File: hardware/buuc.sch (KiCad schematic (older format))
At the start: 18 parts, among them P1 USB_OTG, P2 CONN_01X02, Q1 NDS8434, U1 BOOST_REGULATOR, U2 MCP73842-840I/UN

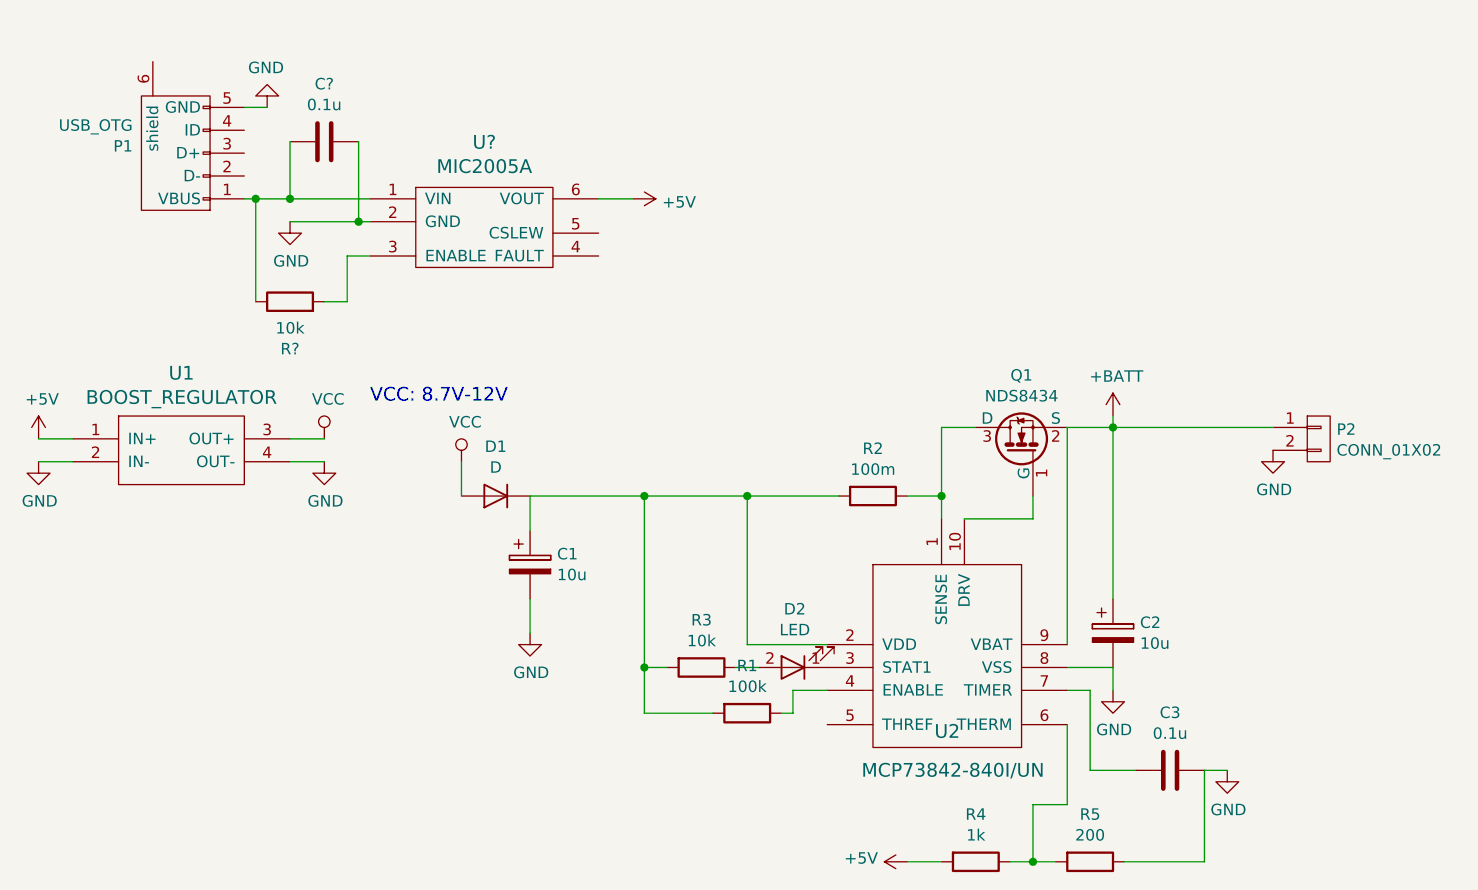
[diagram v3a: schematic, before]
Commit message: Swapping resistor footprint for one that's a bit easier to solder onto a milled board; minor move of the USB connector.
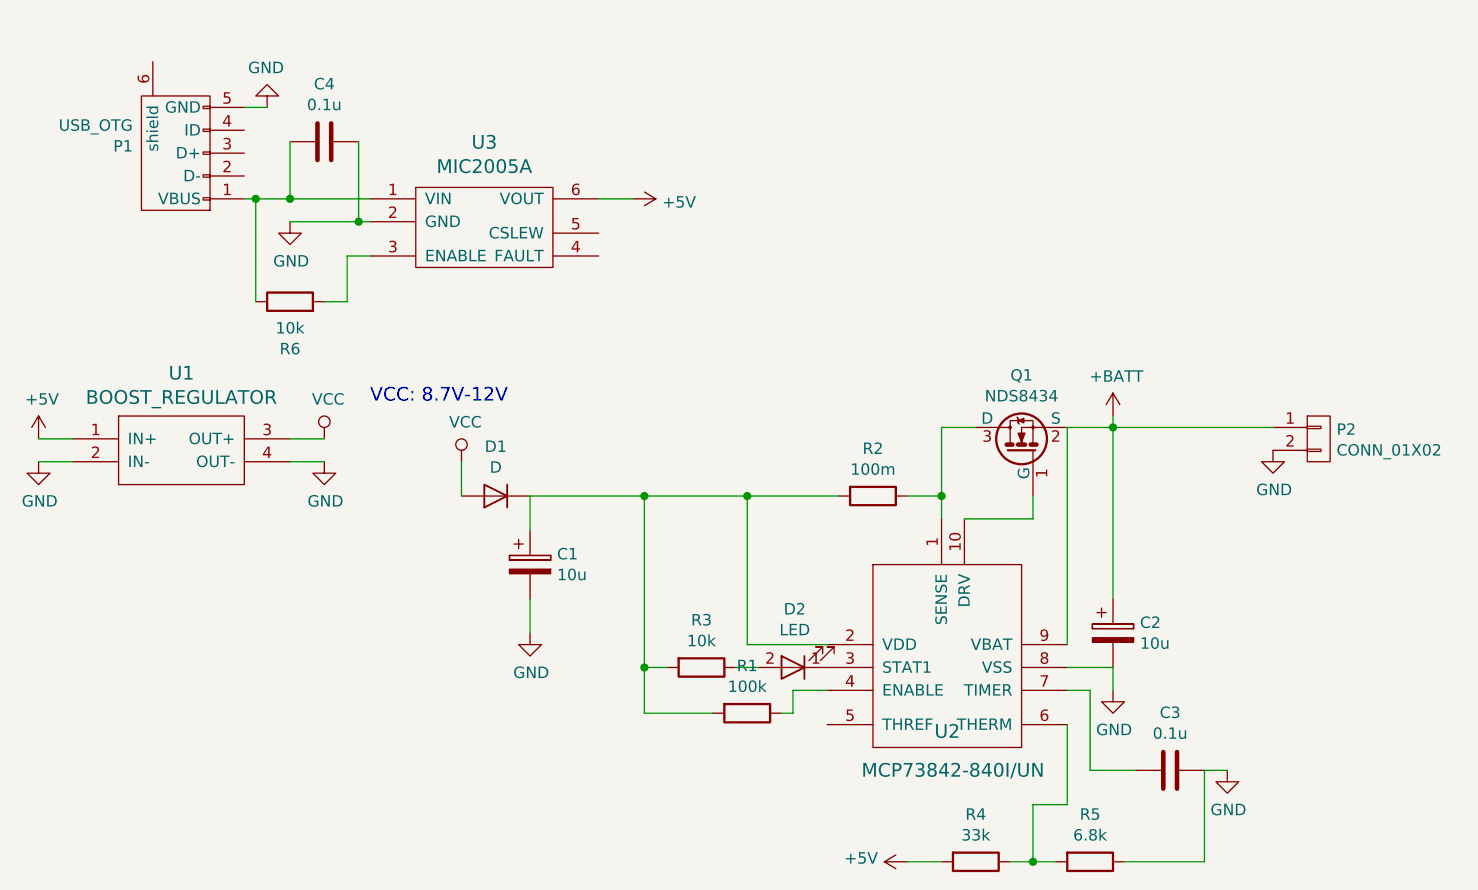
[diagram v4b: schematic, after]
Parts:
- C3: footprint KiCad/Capacitors_SMD.pretty:C_0805_HandSoldering -> coddingtonbear/coddingtonbear.pretty:0805_Milling
- C4: renamed from C?; footprint KiCad/Capacitors_SMD.pretty:C_0805_HandSoldering -> coddingtonbear/coddingtonbear.pretty:0805_Milling
- D2: footprint adamgreig/agg-kicad/agg.pretty:0805-LED -> coddingtonbear/coddingtonbear.pretty:0805_Milling
- R1, R2, R3: footprint apexelectrix/apex-smd-resistors.pretty:R_0805_HandSoldering -> coddingtonbear/coddingtonbear.pretty:0805_Milling
- R4: value 1k -> 33k; footprint apexelectrix/apex-smd-resistors.pretty:R_0805_HandSoldering -> coddingtonbear/coddingtonbear.pretty:0805_Milling
- R5: value 200 -> 6.8k; footprint apexelectrix/apex-smd-resistors.pretty:R_0805_HandSoldering -> coddingtonbear/coddingtonbear.pretty:0805_Milling
- R6: renamed from R?; footprint apexelectrix/apex-smd-resistors.pretty:R_0805_HandSoldering -> coddingtonbear/coddingtonbear.pretty:0805_Milling
- U3: renamed from U?; footprint (none) -> adamgreig/agg-kicad/agg.pretty:SOT-23-6
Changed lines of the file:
@@
 F 0 "R2" V 4393 2950 50  0000 C CNN
 F 1 "100m" V 4484 2950 50  0000 C CNN
-F 2 "apexelectrix/apex-smd-resistors.pretty:R_0805_HandSoldering" V 4530 2950 50  0001 C CNN
+F 2 "coddingtonbear/coddingtonbear.pretty:0805_Milling" V 4530 2950 50  0001 C CNN
 F 3 "" H 4600 2950 50  0000 C CNN
 	1    4600 2950
@@
 F 0 "D2" H 4242 3445 50  0000 C CNN
 F 1 "LED" H 4242 3536 50  0000 C CNN
-F 2 "adamgreig/agg-kicad/agg.pretty:0805-LED" H 4250 3700 50  0001 C CNN
+F 2 "coddingtonbear/coddingtonbear.pretty:0805_Milling" H 4250 3700 50  0001 C CNN
 F 3 "" H 4250 3700 50  0000 C CNN
 	1    4250 3700
@@
 F 0 "R1" V 3843 3900 50  0000 C CNN
 F 1 "100k" V 3934 3900 50  0000 C CNN
-F 2 "apexelectrix/apex-smd-resistors.pretty:R_0805_HandSoldering" V 3980 3900 50  0001 C CNN
+F 2 "coddingtonbear/coddingtonbear.pretty:0805_Milling" V 3980 3900 50  0001 C CNN
 F 3 "" H 4050 3900 50  0000 C CNN
 	1    4050 3900
@@
 F 0 "R3" V 3643 3700 50  0000 C CNN
 F 1 "10k" V 3734 3700 50  0000 C CNN
-F 2 "apexelectrix/apex-smd-resistors.pretty:R_0805_HandSoldering" V 3780 3700 50  0001 C CNN
+F 2 "coddingtonbear/coddingtonbear.pretty:0805_Milling" V 3780 3700 50  0001 C CNN
 F 3 "" H 3850 3700 50  0000 C CNN
 	1    3850 3700
@@
 F 0 "C3" V 5648 4150 50  0000 C CNN
 F 1 "0.1u" V 5739 4150 50  0000 C CNN
-F 2 "KiCad/Capacitors_SMD.pretty:C_0805_HandSoldering" H 5938 4000 50  0001 C CNN
+F 2 "coddingtonbear/coddingtonbear.pretty:0805_Milling" H 5938 4000 50  0001 C CNN
 F 3 "" H 5900 4150 50  0000 C CNN
 	1    5900 4150
@@
 P 5050 4550
 F 0 "R4" V 4843 4550 50  0000 C CNN
-F 1 "1k" V 4934 4550 50  0000 C CNN
-F 2 "apexelectrix/apex-smd-resistors.pretty:R_0805_HandSoldering" V 4980 4550 50  0001 C CNN
+F 1 "33k" V 4934 4550 50  0000 C CNN
+F 2 "coddingtonbear/coddingtonbear.pretty:0805_Milling" V 4980 4550 50  0001 C CNN
 F 3 "" H 5050 4550 50  0000 C CNN
 	1    5050 4550
@@
 P 5550 4550
 F 0 "R5" V 5343 4550 50  0000 C CNN
-F 1 "200" V 5434 4550 50  0000 C CNN
-F 2 "apexelectrix/apex-smd-resistors.pretty:R_0805_HandSoldering" V 5480 4550 50  0001 C CNN
+F 1 "6.8k" V 5434 4550 50  0000 C CNN
+F 2 "coddingtonbear/coddingtonbear.pretty:0805_Milling" V 5480 4550 50  0001 C CNN
 F 3 "" H 5550 4550 50  0000 C CNN
 	1    5550 4550
@@
 	4750 4550 4900 4550
 $Comp
-L MIC2005A U?
+L MIC2005A U3
 U 1 1 59BADA49
 P 2900 1750
-F 0 "U?" H 2900 2097 60  0000 C CNN
+F 0 "U3" H 2900 2097 60  0000 C CNN
 F 1 "MIC2005A" H 2900 1991 60  0000 C CNN
-F 2 "" H 2900 1750 60  0001 C CNN
+F 2 "adamgreig/agg-kicad/agg.pretty:SOT-23-6" H 2900 1750 60  0001 C CNN
 F 3 "" H 2900 1750 60  0001 C CNN
 	1    2900 1750
@@
 	3550 1650 3400 1650
 $Comp
-L GND #PWR?
+L GND #PWR014
 U 1 1 59BADB64
 P 2050 1750
-F 0 "#PWR?" H 2050 1500 50  0001 C CNN
+F 0 "#PWR014" H 2050 1500 50  0001 C CNN
 F 1 "GND" H 2055 1577 50  0000 C CNN
 F 2 "" H 2050 1750 50  0000 C CNN
@@
 	2400 1750 2050 1750
 $Comp
-L R R?
+L R R6
 U 1 1 59BADC60
 P 2050 2100
-F 0 "R?" V 1843 2100 50  0000 C CNN
+F 0 "R6" V 1843 2100 50  0000 C CNN
 F 1 "10k" V 1934 2100 50  0000 C CNN
-F 2 "apexelectrix/apex-smd-resistors.pretty:R_0805_HandSoldering" V 1980 2100 50  0001 C CNN
+F 2 "coddingtonbear/coddingtonbear.pretty:0805_Milling" V 1980 2100 50  0001 C CNN
 F 3 "" H 2050 2100 50  0000 C CNN
 	1    2050 2100
@@
 Connection ~ 1900 1650
 $Comp
-L C C?
+L C C4
 U 1 1 59BAE16D
 P 2200 1400
-F 0 "C?" V 1948 1400 50  0000 C CNN
+F 0 "C4" V 1948 1400 50  0000 C CNN
 F 1 "0.1u" V 2039 1400 50  0000 C CNN
-F 2 "KiCad/Capacitors_SMD.pretty:C_0805_HandSoldering" H 2238 1250 50  0001 C CNN
+F 2 "coddingtonbear/coddingtonbear.pretty:0805_Milling" H 2238 1250 50  0001 C CNN
 F 3 "" H 2200 1400 50  0000 C CNN
 	1    2200 1400

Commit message: Apparently: active low.  FFS.
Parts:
- U3: symbol MIC2005A -> MIC2005A-RESCUE-buuc
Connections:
- net GND: now also R6.1
- net at C4.2, P1.1 (VBUS), U3.1 (VIN): no longer R6.1
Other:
- moved on the sheet: R6
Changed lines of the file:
@@
 EESchema Schematic File Version 2
+LIBS:buuc-rescue
 LIBS:power
 LIBS:device
@@
 	4750 4550 4900 4550
 $Comp
-L MIC2005A U3
+L MIC2005A-RESCUE-buuc U3
 U 1 1 59BADA49
 P 2900 1750
@@
 L GND #PWR014
 U 1 1 59BADB64
-P 2050 1750
-F 0 "#PWR014" H 2050 1500 50  0001 C CNN
-F 1 "GND" H 2055 1577 50  0000 C CNN
-F 2 "" H 2050 1750 50  0000 C CNN
-F 3 "" H 2050 1750 50  0000 C CNN
-	1    2050 1750
-	1    0    0    -1
-$EndComp
-Wire Wire Line
-	2400 1750 2050 1750
+P 1800 2100
+F 0 "#PWR014" H 1800 1850 50  0001 C CNN
+F 1 "GND" H 1805 1927 50  0000 C CNN
+F 2 "" H 1800 2100 50  0000 C CNN
+F 3 "" H 1800 2100 50  0000 C CNN
+	1    1800 2100
+	1    0    0    -1
+$EndComp
+Wire Wire Line
+	1800 1750 2400 1750
 $Comp
 L R R6
 U 1 1 59BADC60
-P 2050 2100
-F 0 "R6" V 1843 2100 50  0000 C CNN
-F 1 "10k" V 1934 2100 50  0000 C CNN
-F 2 "coddingtonbear/coddingtonbear.pretty:0805_Milling" V 1980 2100 50  0001 C CNN
-F 3 "" H 2050 2100 50  0000 C CNN
-	1    2050 2100
-	0    -1   -1   0
-$EndComp
-Wire Wire Line
-	2200 2100 2300 2100
-Wire Wire Line
-	2300 2100 2300 1900
-Wire Wire Line
-	2300 1900 2400 1900
-Wire Wire Line
-	1900 2100 1900 1650
-Connection ~ 1900 1650
+P 2150 1950
+F 0 "R6" V 1943 1950 50  0000 C CNN
+F 1 "10k" V 2034 1950 50  0000 C CNN
+F 2 "coddingtonbear/coddingtonbear.pretty:0805_Milling" V 2080 1950 50  0001 C CNN
+F 3 "" H 2150 1950 50  0000 C CNN
+	1    2150 1950
+	1    0    0    -1
+$EndComp
 $Comp
 L C C4
@@
 	2050 1400 2050 1650
 Connection ~ 2050 1650
+Wire Wire Line
+	2150 1800 2150 1750
+Connection ~ 2150 1750
+Wire Wire Line
+	2150 2100 2400 2100
+Wire Wire Line
+	2400 2100 2400 1900
+Wire Wire Line
+	1800 1750 1800 2100
 $EndSCHEMATC

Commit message: Adding extra pads allowing me to fine-tune the consumed current; adding unpopulated bypass resistor around the MIC2005.
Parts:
- P1: symbol USB_OTG -> USB_OTG-RESCUE-buuc
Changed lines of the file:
@@
 LIBS:contrib
 LIBS:valves
-LIBS:coddingtonbear
 LIBS:buuc-cache
 EELAYER 26 0
@@
 $EndDescr
 $Comp
-L USB_OTG P1
+L USB_OTG-RESCUE-buuc P1
 U 1 1 59AF531F
 P 1550 1450

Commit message: fixup! Adding extra pads allowing me to fine-tune the consumed current; adding unpopulated bypass resistor around the MIC2005.
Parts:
- added R?: 100m, coddingtonbear/coddingtonbear.pretty:0805_Milling, symbol R
- added R? (x7): 0, coddingtonbear/coddingtonbear.pretty:0805_Milling, symbol R
- added R?: EMPTY, coddingtonbear/coddingtonbear.pretty:0805_Milling, symbol R
- R2: value 100m -> 0
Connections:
- net +5V: now also R?.2
- net at C4.2, P1.1 (VBUS), U3.1 (VIN): now also R?.1
- net at Q1.3 (D), U2.1 (SENSE): now also R?.2; no longer R2.1
- net at C1.1, D1.1 (K), R1.2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: now also R?.1; no longer R2.2
- new net: R2.1, R?.2
- new net: R2.2, R?.2
- new net: R?.1, R?.2 (x5)
- new net: R?.1, R?.1
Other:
- moved on the sheet: R2
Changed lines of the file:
@@
 L R R2
 U 1 1 59AF69FF
-P 4600 2950
-F 0 "R2" V 4393 2950 50  0000 C CNN
-F 1 "100m" V 4484 2950 50  0000 C CNN
-F 2 "coddingtonbear/coddingtonbear.pretty:0805_Milling" V 4530 2950 50  0001 C CNN
-F 3 "" H 4600 2950 50  0000 C CNN
-	1    4600 2950
-	0    1    1    0
+P 3950 1900
+F 0 "R2" V 3743 1900 50  0000 C CNN
+F 1 "0" V 3834 1900 50  0000 C CNN
+F 2 "coddingtonbear/coddingtonbear.pretty:0805_Milling" V 3880 1900 50  0001 C CNN
+F 3 "" H 3950 1900 50  0000 C CNN
+	1    3950 1900
+	-1   0    0    1
 $EndComp
 $Comp
@@
 Connection ~ 3600 3700
 Wire Wire Line
-	3100 2950 4450 2950
-Wire Wire Line
 	4400 3600 4050 3600
 Wire Wire Line
 	4050 3600 4050 2950
-Connection ~ 4050 2950
-Wire Wire Line
-	4750 2950 4900 2950
-Wire Wire Line
-	4900 2650 4900 3050
+Wire Wire Line
+	4900 1750 4900 3050
 $Comp
 L NDS8434 Q1
@@
 Wire Wire Line
 	4900 2650 5050 2650
-Connection ~ 4900 2950
 Wire Wire Line
 	5450 3600 5450 2650
@@
 Wire Wire Line
 	1800 1750 1800 2100
+$Comp
+L R R?
+U 1 1 59C097A1
+P 3950 2700
+F 0 "R?" V 3743 2700 50  0000 C CNN
+F 1 "100m" V 3834 2700 50  0000 C CNN
+F 2 "coddingtonbear/coddingtonbear.pretty:0805_Milling" V 3880 2700 50  0001 C CNN
+F 3 "" H 3950 2700 50  0000 C CNN
+	1    3950 2700
+	-1   0    0    1
+$EndComp
+$Comp
+L R R?
+U 1 1 59C0980C
+P 3950 2300
+F 0 "R?" V 3743 2300 50  0000 C CNN
+F 1 "0" V 3834 2300 50  0000 C CNN
+F 2 "coddingtonbear/coddingtonbear.pretty:0805_Milling" V 3880 2300 50  0001 C CNN
+F 3 "" H 3950 2300 50  0000 C CNN
+	1    3950 2300
+	-1   0    0    1
+$EndComp
+$Comp
+L R R?
+U 1 1 59C09A2E
+P 4300 2700
+F 0 "R?" V 4093 2700 50  0000 C CNN
+F 1 "0" V 4184 2700 50  0000 C CNN
+F 2 "coddingtonbear/coddingtonbear.pretty:0805_Milling" V 4230 2700 50  0001 C CNN
+F 3 "" H 4300 2700 50  0000 C CNN
+	1    4300 2700
+	-1   0    0    1
+$EndComp
+$Comp
+L R R?
+U 1 1 59C09A8A
+P 4300 2300
+F 0 "R?" V 4093 2300 50  0000 C CNN
+F 1 "0" V 4184 2300 50  0000 C CNN
+F 2 "coddingtonbear/coddingtonbear.pretty:0805_Milling" V 4230 2300 50  0001 C CNN
+F 3 "" H 4300 2300 50  0000 C CNN
+	1    4300 2300
+	-1   0    0    1
+$EndComp
+$Comp
+L R R?
+U 1 1 59C09AD2
+P 4300 1900
+F 0 "R?" V 4093 1900 50  0000 C CNN
+F 1 "0" V 4184 1900 50  0000 C CNN
+F 2 "coddingtonbear/coddingtonbear.pretty:0805_Milling" V 4230 1900 50  0001 C CNN
+F 3 "" H 4300 1900 50  0000 C CNN
+	1    4300 1900
+	-1   0    0    1
+$EndComp
+$Comp
+L R R?
+U 1 1 59C09B3C
+P 4650 2700
+F 0 "R?" V 4443 2700 50  0000 C CNN
+F 1 "0" V 4534 2700 50  0000 C CNN
+F 2 "coddingtonbear/coddingtonbear.pretty:0805_Milling" V 4580 2700 50  0001 C CNN
+F 3 "" H 4650 2700 50  0000 C CNN
+	1    4650 2700
+	-1   0    0    1
+$EndComp
+$Comp
+L R R?
+U 1 1 59C0A0C4
+P 4650 2300
+F 0 "R?" V 4443 2300 50  0000 C CNN
+F 1 "0" V 4534 2300 50  0000 C CNN
+F 2 "coddingtonbear/coddingtonbear.pretty:0805_Milling" V 4580 2300 50  0001 C CNN
+F 3 "" H 4650 2300 50  0000 C CNN
+	1    4650 2300
+	-1   0    0    1
+$EndComp
+$Comp
+L R R?
+U 1 1 59C0A112
+P 4650 1900
+F 0 "R?" V 4443 1900 50  0000 C CNN
+F 1 "0" V 4534 1900 50  0000 C CNN
+F 2 "coddingtonbear/coddingtonbear.pretty:0805_Milling" V 4580 1900 50  0001 C CNN
+F 3 "" H 4650 1900 50  0000 C CNN
+	1    4650 1900
+	-1   0    0    1
+$EndComp
+Wire Wire Line
+	4050 2950 3100 2950
+Wire Wire Line
+	3950 2950 3950 2850
+Connection ~ 3950 2950
+Wire Wire Line
+	3950 2550 3950 2450
+Wire Wire Line
+	3950 2150 3950 2050
+Wire Wire Line
+	3950 1750 4300 1750
+Wire Wire Line
+	4300 2050 4300 2150
+Wire Wire Line
+	4300 2450 4300 2550
+Wire Wire Line
+	4300 2850 4300 2950
+Wire Wire Line
+	4300 2950 4650 2950
+Wire Wire Line
+	4650 2950 4650 2850
+Wire Wire Line
+	4650 2550 4650 2450
+Wire Wire Line
+	4650 2150 4650 2050
+Wire Wire Line
+	4650 1750 4900 1750
+Connection ~ 4900 2650
+$Comp
+L R R?
+U 1 1 59C0A9C6
+P 2900 1100
+F 0 "R?" V 2693 1100 50  0000 C CNN
+F 1 "EMPTY" V 2784 1100 50  0000 C CNN
+F 2 "coddingtonbear/coddingtonbear.pretty:0805_Milling" V 2830 1100 50  0001 C CNN
+F 3 "" H 2900 1100 50  0000 C CNN
+	1    2900 1100
+	0    -1   -1   0
+$EndComp
+Wire Wire Line
+	2400 1650 2400 1100
+Wire Wire Line
+	2400 1100 2750 1100
+Wire Wire Line
+	3050 1100 3500 1100
+Wire Wire Line
+	3500 1100 3500 1650
+Connection ~ 3500 1650
 $EndSCHEMATC
